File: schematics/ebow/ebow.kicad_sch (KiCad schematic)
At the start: 8 parts, among them U1 LM386

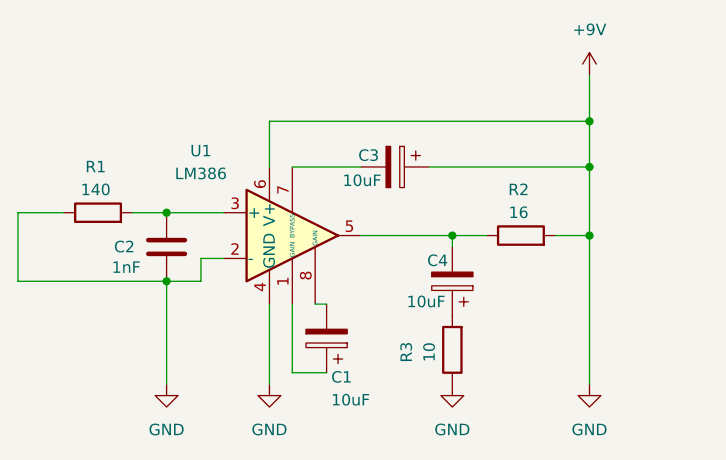
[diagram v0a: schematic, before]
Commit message: fixed capacitors, added low and high pass filters, added led indicator
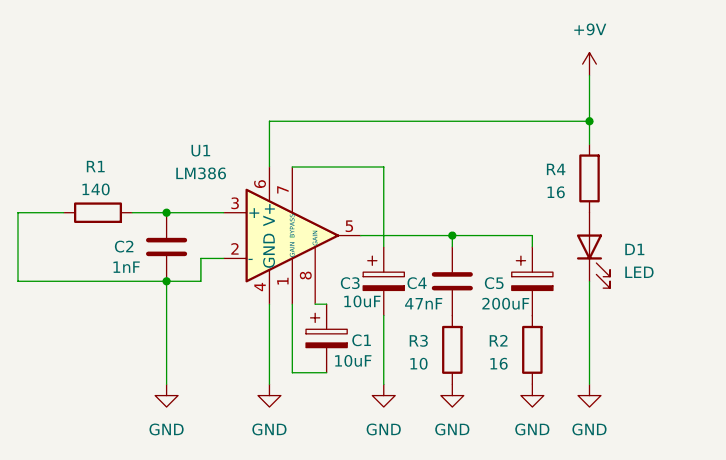
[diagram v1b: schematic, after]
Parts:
- removed C4: 10uF, symbol Device:C_Polarized
- added C4: 47nF, symbol Device:C
- added C5: 200uF, symbol Device:C_Polarized
- added D1: LED, symbol Device:LED
- added R4: 16, symbol Device:R
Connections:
- net +9V: now also R4.2; no longer C2.2, C3.1, R1.1, R2.2, R3.1, U1.2 (-), U1.4 (GND)
- net at C1.1: now also U1.8 (GAIN); no longer U1.1 (GAIN)
- net at C1.2: now also U1.1 (GAIN); no longer U1.8 (GAIN)
- net at R3.2: now also C4.2
- net at U1.5: now also C4.1, C5.1; no longer R2.1
- net at U1.7 (BYPASS): now also C3.1; no longer C3.2
- new net: D1.2 (A), R4.1
- new net: C5.2, R2.2
- new net GND: C2.2, C3.2, D1.1 (K), R1.1, R2.1, R3.1, U1.2 (-), U1.4 (GND)
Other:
- moved on the sheet: C1, C3, R2

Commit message: using inductors to represent coils
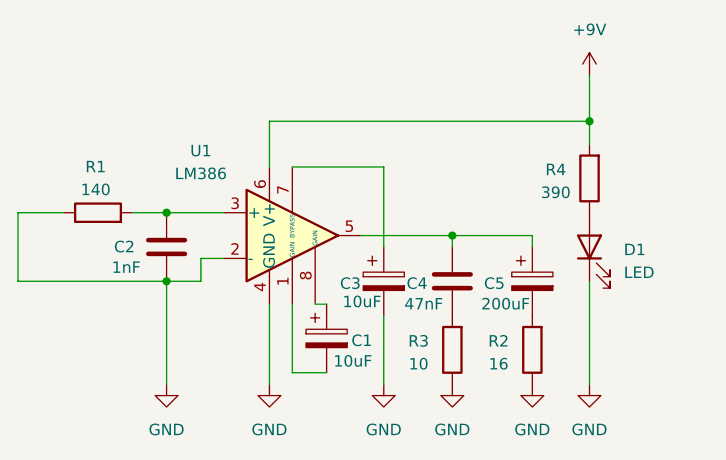
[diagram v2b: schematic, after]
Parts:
- R4: value 16 -> 390
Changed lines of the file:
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@@
 			)
 		)
-		(property "Value" "16"
+		(property "Value" "390"
 			(at 158.8135 90.4875 0)
 			(effects

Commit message: added custom symbol for input and output coils
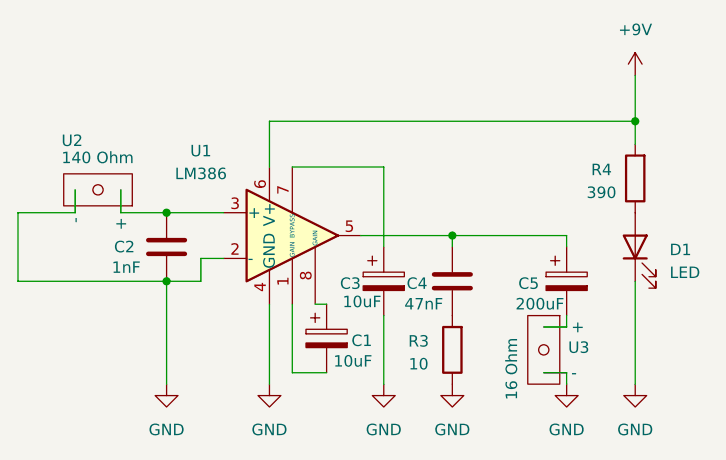
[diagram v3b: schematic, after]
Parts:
- removed R1: 140, symbol Device:R
- removed R2: 16, symbol Device:R
- added U2: 140 Ohm, symbol Ebow_custom_sym:Coil
- added U3: 16 Ohm, symbol Ebow_custom_sym:Coil
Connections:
- net GND: now also U2. (-), U3. (-)
- net at C2.1, U1.3 (+): now also U2. (-)
- net at C5.2: now also U3. (-)
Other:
- moved on the sheet: C5, D1, R4
